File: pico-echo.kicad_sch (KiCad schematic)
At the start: 55 parts, among them J1 USB_C_Receptacle_USB2.0, J2 I2C, J4 Conn, J5 Conn, J6 BAT, J7 PICO Probe, Q1 BSS83P, SW1 SW_Push, SW2 SW_Push, U1 RP2040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

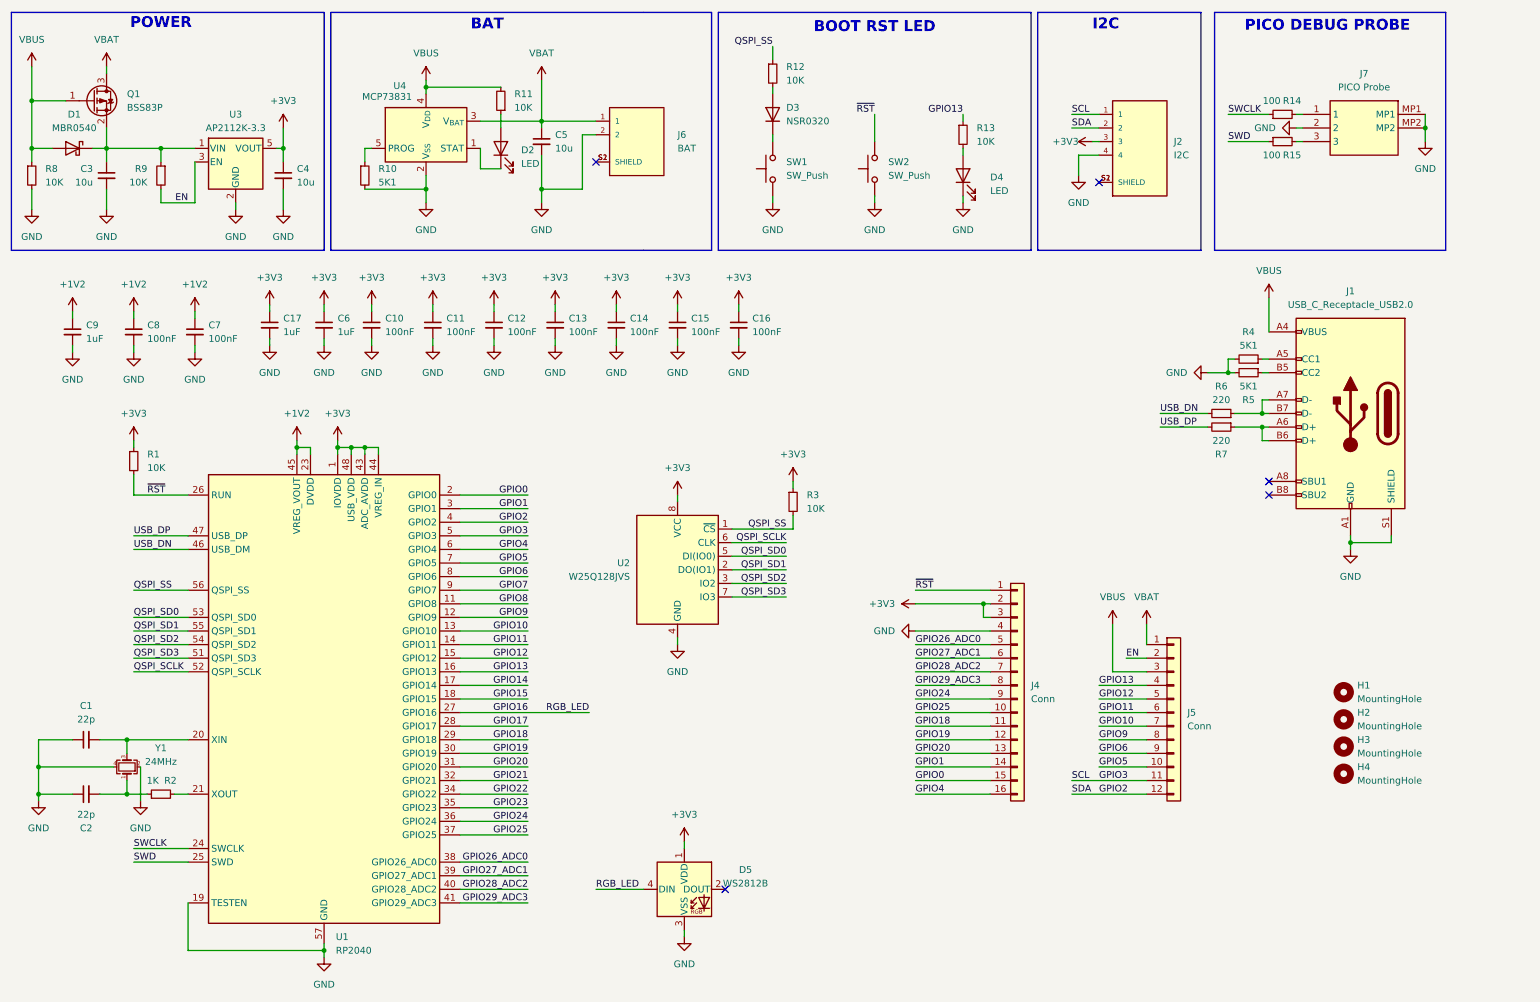
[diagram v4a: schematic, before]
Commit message: Add B.O.M to the schematic (not finished yet)
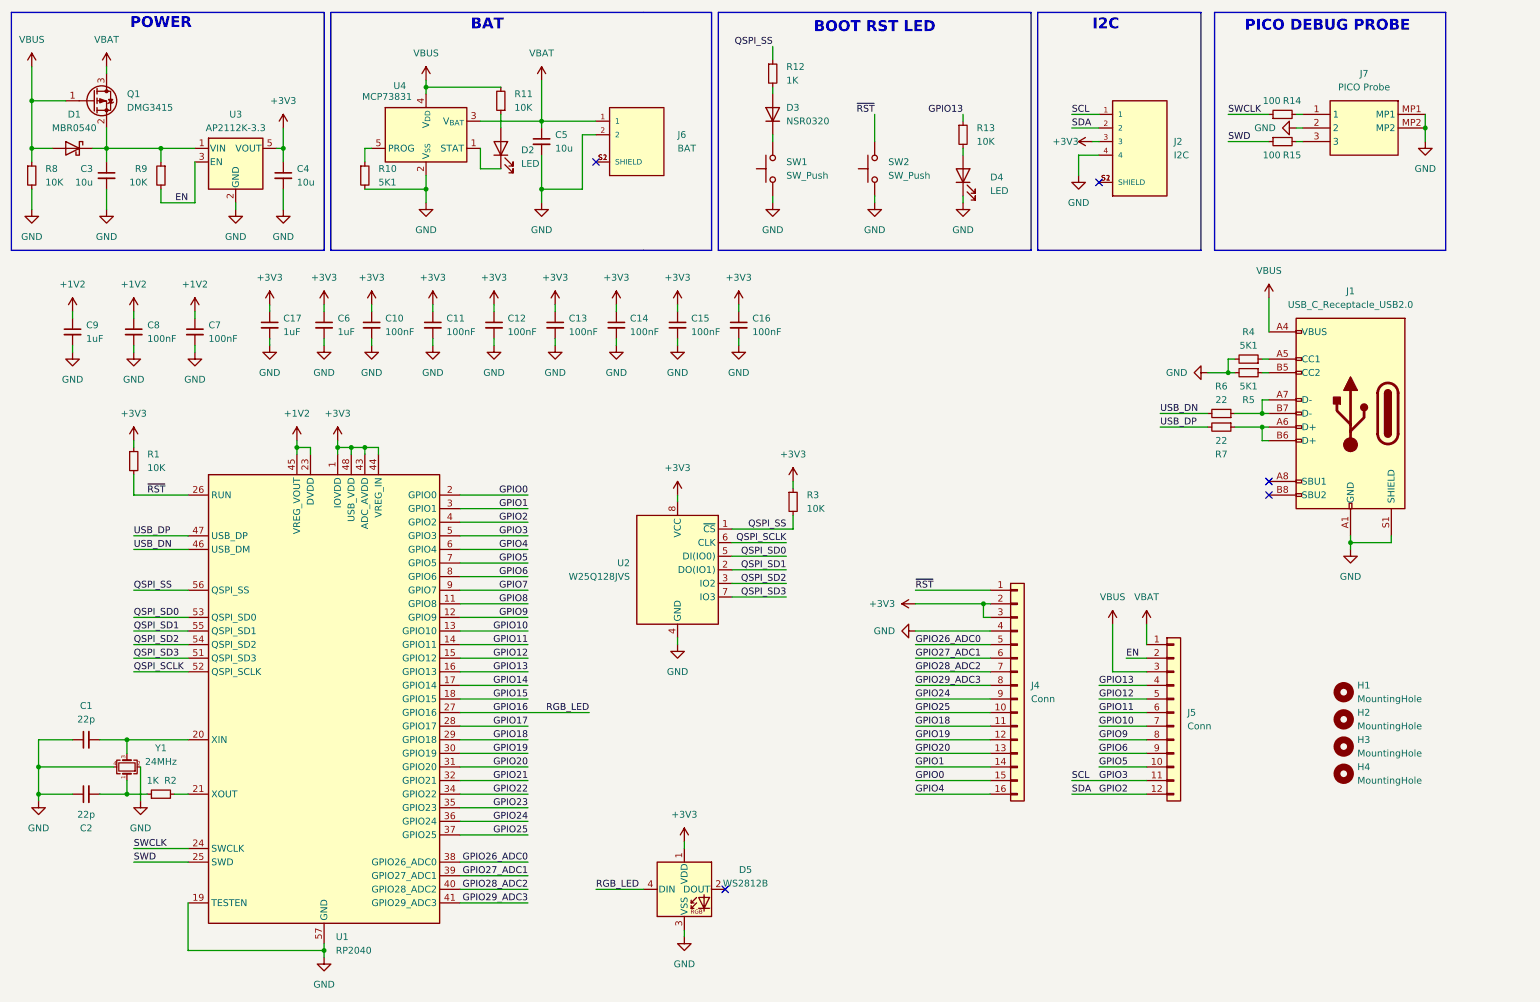
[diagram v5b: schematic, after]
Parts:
- C1, C2: JLCPCB Part # (none) -> C1555
- C10, C11, C12, C13, C14, C15, C16, C7, C8: JLCPCB Part # (none) -> C307331
- C17, C6, C9: JLCPCB Part # (none) -> C15849
- C3, C4, C5: JLCPCB Part # (none) -> C96446
- Q1: value BSS83P -> DMG3415
- R1, R11, R13, R3, R8, R9: JLCPCB Part # (none) -> C25744
- R10, R4, R5: JLCPCB Part # (none) -> C25905
- R12: value 10K -> 1K; JLCPCB Part # (none) -> C11702
- R14, R15: JLCPCB Part # (none) -> C25076
- R2: JLCPCB Part # (none) -> C11702
- R6, R7: value 220 -> 22; JLCPCB Part # (none) -> C25092
- U1: JLCPCB Part # (none) -> RP2040
- U3: JLCPCB Part # (none) -> C51118
- U4: JLCPCB Part # (none) -> C424093
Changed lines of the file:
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@@
 			)
 		)
-		(property "JLCPCB Part #" ""
+		(property "JLCPCB Part #" "C307331"
 			(at 127 72.39 0)
 			(effects
@@
 			)
 		)
-		(property "JLCPCB Part #" ""
+		(property "JLCPCB Part #" "C25905"
 			(at 80.01 44.45 0)
 			(effects
@@
 			)
 		)
-		(property "JLCPCB Part #" ""
+		(property "JLCPCB Part #" "C96446"
 			(at 113.03 38.1 0)
 			(effects
@@
 			)
 		)
-		(property "JLCPCB Part #" ""
+		(property "JLCPCB Part #" "C25076"
 			(at 251.46 38.1 0)
 			(effects
@@
 			)
 		)
-		(property "JLCPCB Part #" ""
+		(property "JLCPCB Part #" "C307331"
 			(at 104.14 72.39 0)
 			(effects
@@
 			)
 		)
-		(property "JLCPCB Part #" ""
+		(property "JLCPCB Part #" "C307331"
 			(at 115.57 72.39 0)
 			(effects
@@
 			)
 		)
-		(property "JLCPCB Part #" ""
+		(property "JLCPCB Part #" "C307331"
 			(at 81.28 72.39 0)
 			(effects
@@
 			)
 		)
-		(property "Value" "220"
+		(property "Value" "22"
 			(at 240.03 93.98 90)
 			(effects
@@
 			)
 		)
-		(property "JLCPCB Part #" ""
+		(property "JLCPCB Part #" "C25092"
 			(at 240.03 91.44 0)
 			(effects
@@
 			)
 		)
-		(property "JLCPCB Part #" ""
+		(property "JLCPCB Part #" "C307331"
 			(at 36.83 73.66 0)
 			(effects
@@
 			)
 		)
-		(property "JLCPCB Part #" ""
+		(property "JLCPCB Part #" "C51118"
 			(at 55.88 41.91 0)
 			(effects
@@
 			)
 		)
-		(property "JLCPCB Part #" ""
+		(property "JLCPCB Part #" "C25076"
 			(at 251.46 33.02 0)
 			(effects
@@
 			)
 		)
-		(property "JLCPCB Part #" ""
+		(property "JLCPCB Part #" "C25744"
 			(at 160.02 105.41 0)
 			(effects
@@
 			)
 		)
-		(property "JLCPCB Part #" ""
+		(property "JLCPCB Part #" "C25905"
 			(at 245.11 78.74 0)
 			(effects
@@
 			)
 		)
-		(property "Value" "BSS83P"
+		(property "Value" "DMG3415"
 			(at 35.56 31.7499 0)
 			(effects
@@
 			)
 		)
-		(property "JLCPCB Part #" ""
+		(property "JLCPCB Part #" "C25744"
 			(at 191.77 36.83 0)
 			(effects
@@
 			)
 		)
-		(property "JLCPCB Part #" ""
+		(property "JLCPCB Part #" "C424093"
 			(at 91.44 36.83 0)
 			(effects
@@
 			)
 		)
-		(property "JLCPCB Part #" ""
+		(property "JLCPCB Part #" "C15849"
 			(at 62.23 72.39 0)
 			(effects
@@
 			)
 		)
-		(property "Value" "220"
+		(property "Value" "22"
 			(at 240.03 86.36 90)
 			(effects
@@
 			)
 		)
-		(property "JLCPCB Part #" ""
+		(property "JLCPCB Part #" "C25092"
 			(at 240.03 88.9 0)
 			(effects
@@
 			)
 		)
-		(property "JLCPCB Part #" ""
+		(property "JLCPCB Part #" "C307331"
 			(at 138.43 72.39 0)
 			(effects
@@
 			)
 		)
-		(property "JLCPCB Part #" ""
+		(property "JLCPCB Part #" "C307331"
 			(at 92.71 72.39 0)
 			(effects
@@
 			)
 		)
-		(property "JLCPCB Part #" ""
+		(property "JLCPCB Part #" "C1555"
 			(at 27.94 149.86 0)
 			(effects
@@
 			)
 		)
-		(property "JLCPCB Part #" ""
+		(property "JLCPCB Part #" "C25744"
 			(at 17.78 44.45 0)
 			(effects
@@
 			)
 		)
-		(property "JLCPCB Part #" ""
+		(property "JLCPCB Part #" "C1555"
 			(at 27.94 160.02 0)
 			(effects
@@
 			)
 		)
-		(property "JLCPCB Part #" ""
+		(property "JLCPCB Part #" "C307331"
 			(at 149.86 72.39 0)
 			(effects
@@
 			)
 		)
-		(property "JLCPCB Part #" ""
+		(property "JLCPCB Part #" "C25744"
 			(at 36.83 97.79 0)
 			(effects
@@
 			)
 		)
-		(property "JLCPCB Part #" ""
+		(property "JLCPCB Part #" "C15849"
 			(at 72.39 72.39 0)
 			(effects
@@
 			)
 		)
-		(property "JLCPCB Part #" ""
+		(property "JLCPCB Part #" "C96446"
 			(at 64.77 44.45 0)
 			(effects
@@
 			)
 		)
-		(property "Value" "10K"
+		(property "Value" "1K"
 			(at 158.75 26.6699 0)
 			(effects
@@
 			)
 		)
-		(property "JLCPCB Part #" ""
+		(property "JLCPCB Part #" "C11702"
 			(at 156.21 25.4 0)
 			(effects
@@
 			)
 		)
-		(property "JLCPCB Part #" ""
+		(property "JLCPCB Part #" "RP2040"
 			(at 72.39 142.24 0)
 			(effects
@@
 			)
 		)
-		(property "JLCPCB Part #" ""
+		(property "JLCPCB Part #" "C25744"
 			(at 105.41 30.48 0)
 			(effects
@@
 			)
 		)
-		(property "JLCPCB Part #" ""
+		(property "JLCPCB Part #" "C96446"
 			(at 31.75 44.45 0)
 			(effects
@@
 			)
 		)
-		(property "JLCPCB Part #" ""
+		(property "JLCPCB Part #" "C25744"
 			(at 41.91 44.45 0)
 			(effects
@@
 			)
 		)
-		(property "JLCPCB Part #" ""
+		(property "JLCPCB Part #" "C11702"
 			(at 41.91 160.02 0)
 			(effects
@@
 			)
 		)
-		(property "JLCPCB Part #" ""
+		(property "JLCPCB Part #" "C15849"
 			(at 25.4 73.66 0)
 			(effects
@@
 			)
 		)
-		(property "JLCPCB Part #" ""
+		(property "JLCPCB Part #" "C307331"
 			(at 48.26 73.66 0)
 			(effects
@@
 			)
 		)
-		(property "JLCPCB Part #" ""
+		(property "JLCPCB Part #" "C25905"
 			(at 245.11 81.28 0)
 			(effects
